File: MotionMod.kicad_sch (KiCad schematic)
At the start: 20 parts, among them J1 HC-SR04 Ultrasonic, J2 Photoelectric Module, J3 MCP4728 12 Bit DAC, J4 CV Out 1, J5 CV Out 2, J6 CV Out 3, J7 CV Out 4, J8 AMS1117 3.3v Regulator, J9 Eurorack Power, U1 TL074

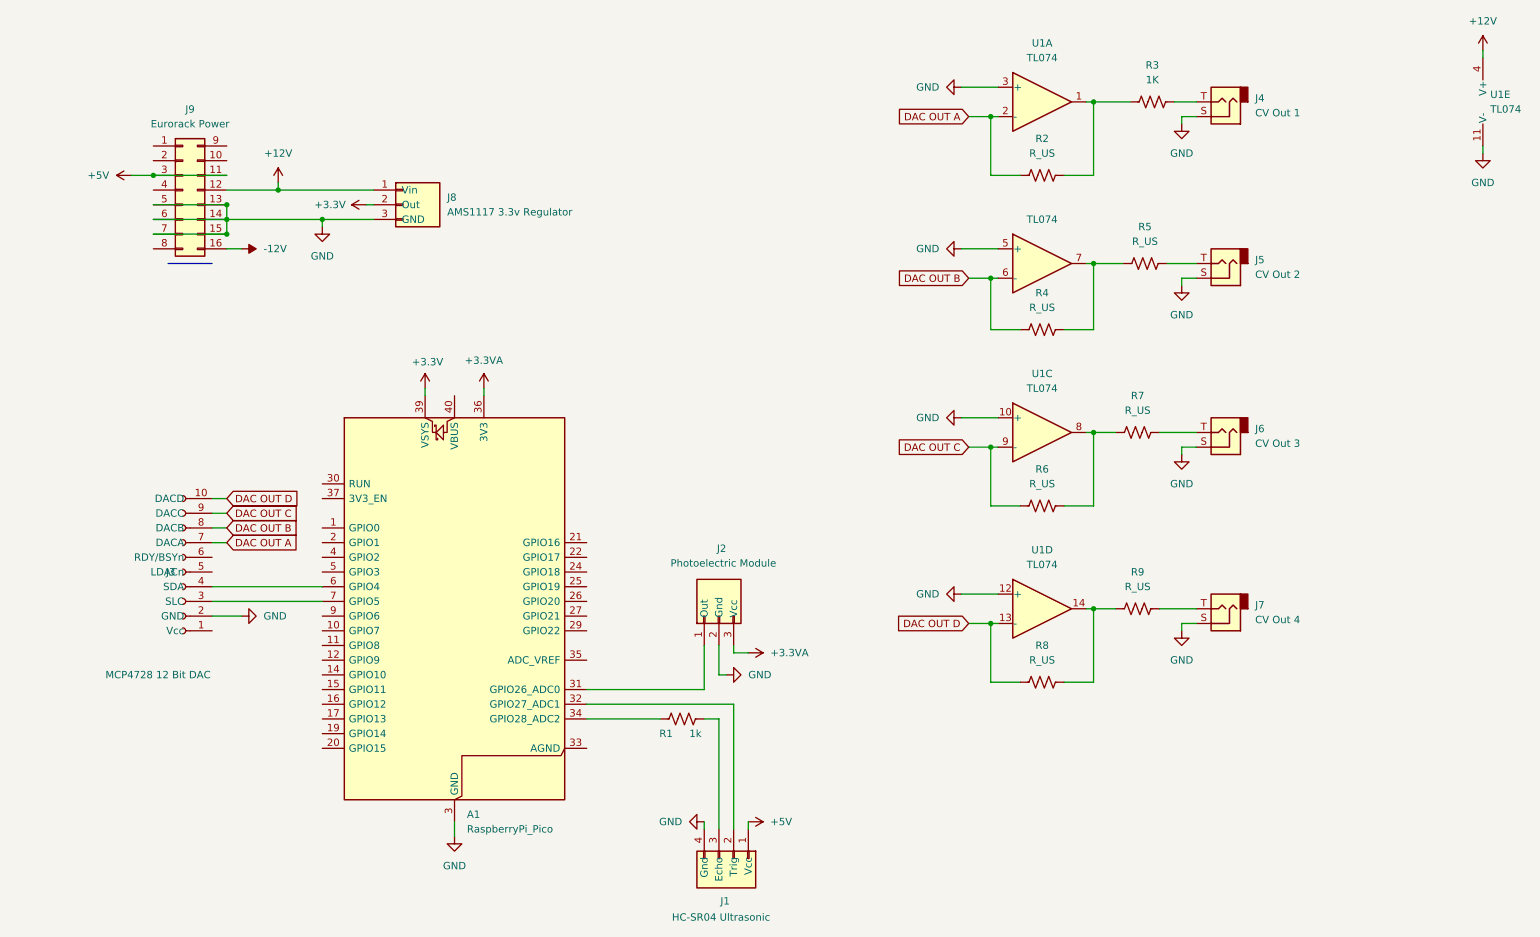
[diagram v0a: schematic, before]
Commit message: added sch image and pdf
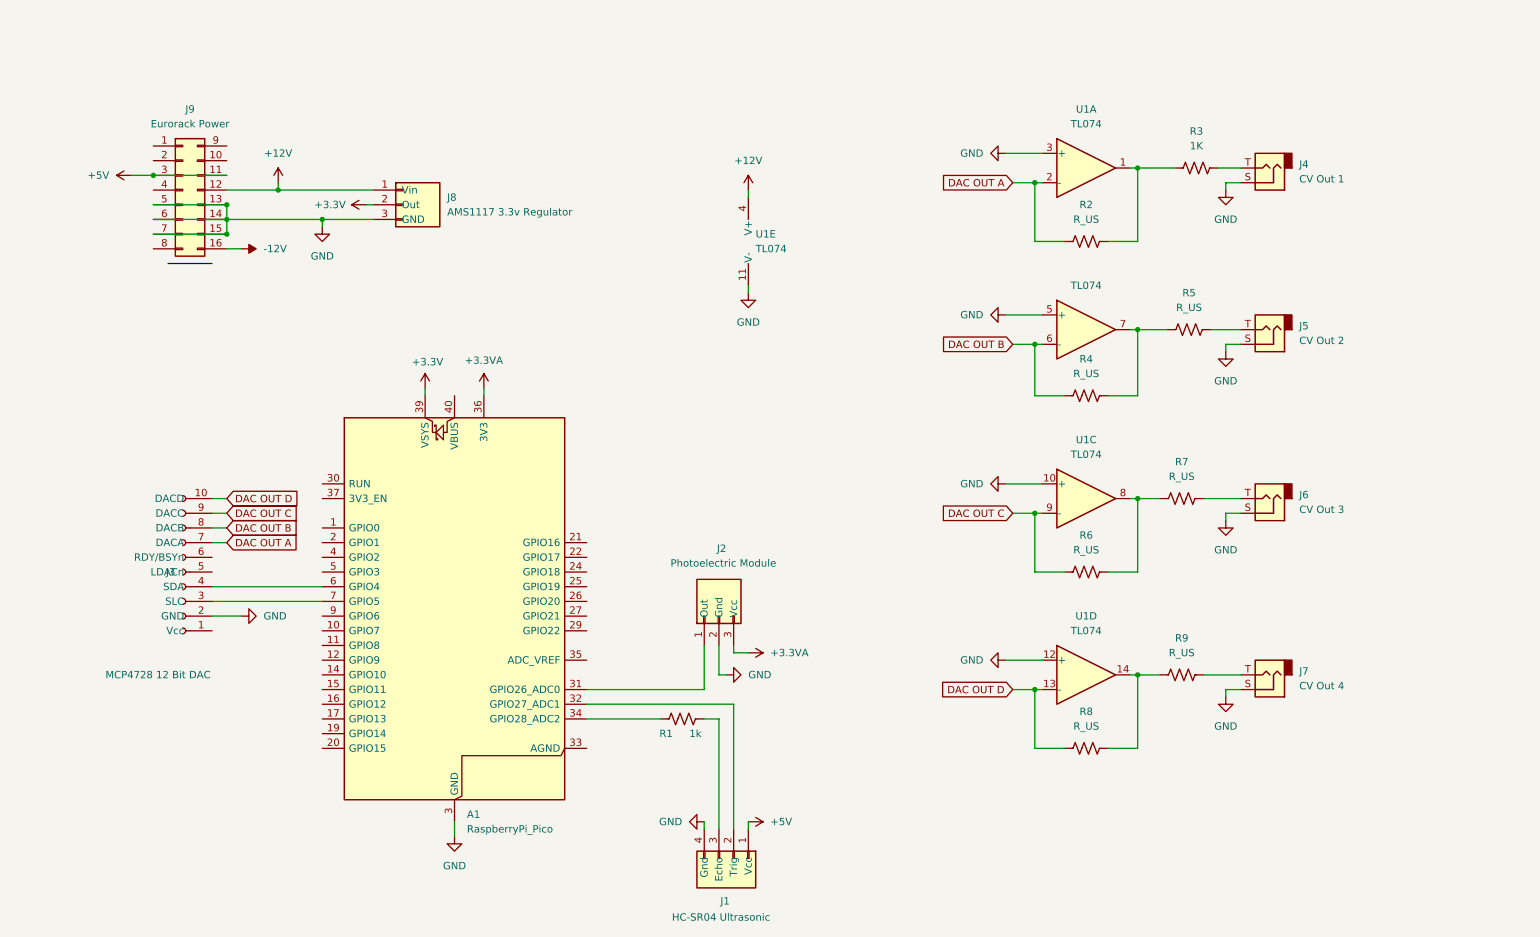
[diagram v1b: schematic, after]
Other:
- title: MotionMod - Movement based CV Generator -> ModSense - Movement based CV Generator for Eurorack
- moved on the sheet: J4, J5, J6, J7, R2, R3, R4, R5, R6, R7, R8, R9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

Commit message: final gerbers for v1
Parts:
- removed J1: HC-SR04 Ultrasonic, symbol Connector_Generic:Conn_01x04
- removed J2: Photoelectric Module, symbol Connector_Generic:Conn_01x03
- removed J4: CV Out 1, symbol Connector_Audio:AudioJack2
- removed J5: CV Out 2, symbol Connector_Audio:AudioJack2
- removed J6: CV Out 3, symbol Connector_Audio:AudioJack2
- removed J7: CV Out 4, symbol Connector_Audio:AudioJack2
- removed J8: AMS1117 3.3v Regulator, symbol Connector_Generic:Conn_01x03
- removed R1: 1k, symbol Device:R_US
- removed R3: 1K, symbol Device:R_US
- removed R5, R7, R9: R_US, symbol Device:R_US
- added J13: BottomSocket1, Connector_PinSocket_2.54mm:PinSocket_1x10_P2.54mm_Vertical, symbol Connector:Conn_01x10_Socket
- added J14: TopHeader1, Connector_PinHeader_2.54mm:PinHeader_1x10_P2.54mm_Vertical, symbol Connector:Conn_01x10_Pin
- added J4: BottomSocket2, Connector_PinSocket_2.54mm:PinSocket_1x10_P2.54mm_Vertical, symbol Connector:Conn_01x10_Socket
- added J5: TopHeader2, Connector_PinHeader_2.54mm:PinHeader_1x10_P2.54mm_Vertical, symbol Connector:Conn_01x10_Pin
- added R10, R12, R20, R21, R22: 10K, PCM_4ms_Resistor:R_Axial_DIN0207_L6.3mm_D2.5mm_P7.62mm_Horizontal, symbol Device:R_US
- added R11: 24K, PCM_4ms_Resistor:R_Axial_DIN0207_L6.3mm_D2.5mm_P7.62mm_Horizontal, symbol Device:R_US
- A1: footprint Module:RaspberryPi_Pico_Common_Unspecified -> Module:RaspberryPi_Pico_SMD_HandSolder
- J2: renamed from J9; value Eurorack Power -> Power; footprint (none) -> PCM_4ms_Connector:Pins_2x08_2.54mm_TH_EuroPower; symbol Connector_Generic:Conn_02x08_Top_Bottom -> PCM_4ms_Connector:Eurorack_Power_16pin_Unshrouded; Manufacturer (none) -> TAD; Part Number (none) -> 1-1602FBV0T; Specifications (none) -> Header, Male Pins, 2*8, spacing 2.54mm, straight pin
- J3: footprint (none) -> Connector_PinHeader_2.54mm:PinHeader_1x10_P2.54mm_Vertical
- R2, R4, R6, R8: value R_US -> 20K; footprint (none) -> PCM_4ms_Resistor:R_Axial_DIN0207_L6.3mm_D2.5mm_P7.62mm_Horizontal
- U1: footprint (none) -> Package_DIP:DIP-14_W7.62mm_LongPads
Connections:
- net +3.3V is gone; now on net +5V: A1.39 (VSYS)
- net +12V: now also J2.7 (12V), J2.8 (+12V); no longer J2.12 (Pin_12)
- net +5V: now also J2.5 (+12V), J2.6 (P6), J3.1 (Vcc), J4.10 (Pin_10), R11.1; no longer J2.11 (Pin_11), J2.3 (Pin_3)
- net -12V: now also J2.15 (-12V), U1.11 (V-)
- net DAC OUT A: now also R21.1; no longer R2.1, U1.2 (-)
- net DAC OUT B: now also R22.1; no longer R4.1, U1.6 (-)
- net DAC OUT C: now also R10.1; no longer R6.1, U1.9 (-)
- net DAC OUT D: now also R20.1; no longer R8.1, U1.13 (-)
- net GND: now also J2.10 (GND), J2.11 (GND), J2.12 (GND), J2.9 (GND), J4.9 (Pin_9), R12.1; no longer J2.15 (Pin_15), J2.5 (Pin_5), J2.6 (Pin_6), J2.7 (Pin_7), U1.10 (+), U1.11 (V-), U1.12 (+), U1.3 (+), U1.5 (+)
- net EncA_s: now reaches A1.1 (GPIO0)
- net EncA_s: now also J4.1 (Pin_1)
- net EncB_s: now reaches A1.2 (GPIO1)
- net EncB_s: now also J4.2 (Pin_2)
- net at A1.21 (GPIO16): now also J13.1 (Pin_1)
- net at A1.22 (GPIO17): now also J13.2 (Pin_2)
- net at A1.24 (GPIO18): now also J13.3 (Pin_3)
- net at A1.25 (GPIO19): now also J13.4 (Pin_4)
- net at A1.26 (GPIO20): now also J13.5 (Pin_5)
- net at A1.27 (GPIO21): now also J13.6 (Pin_6)
- net at A1.29 (GPIO22): now also J13.7 (Pin_7)
- net at A1.31 (GPIO26_ADC0): now also J13.8 (Pin_8)
- net at A1.32 (GPIO27_ADC1): now also J13.9 (Pin_9)
- net at A1.34 (GPIO28_ADC2): now also J13.10 (Pin_10)
- net EncSw_s: now reaches A1.4 (GPIO2)
- net EncSw_s: now also J4.3 (Pin_3)
- net at R2.2, U1.1: now also J4.4 (Pin_4)
- net at R6.2, U1.8: now also J4.6 (Pin_6)
- net at R4.2, U1.7: now also J4.5 (Pin_5)
- net at R8.2, U1.14: now also J4.7 (Pin_7)
- new net: R21.2, R6.1, U1.9 (-)
- new net: R22.2, R8.1, U1.13 (-)
- new net: R10.2, R2.1, U1.2 (-)
- new net: R20.2, R4.1, U1.6 (-)
- new net EncA_p: J5.1 (Pin_1)
- new net Top Board/5V: J5.10 (Pin_10)
- new net Top Board/CV1: J5.4 (Pin_4)
- new net Top Board/CV2: J5.5 (Pin_5)
- new net Top Board/CV3: J5.6 (Pin_6)
- new net Top Board/CV4: J5.7 (Pin_7)
- new net Top Board/DispA: J14.1 (Pin_1)
- new net Top Board/DispB: J14.2 (Pin_2)
- new net Top Board/DispC: J14.3 (Pin_3)
- new net Top Board/DispD: J14.4 (Pin_4)
- new net Top Board/DispDot: J14.8 (Pin_8)
- new net Top Board/DispE: J14.5 (Pin_5)
- new net Top Board/DispF: J14.6 (Pin_6)
- new net Top Board/DispG: J14.7 (Pin_7)
- new net Top Board/Echo: J14.10 (Pin_10)
- new net Top Board/EncB: J5.2 (Pin_2)
- new net Top Board/EncSW: J5.3 (Pin_3)
- new net Top Board/GND: J5.9 (Pin_9)
- new net Top Board/Trig: J14.9 (Pin_9)
- new net Vref: R11.2, R12.2, U1.10 (+), U1.12 (+), U1.3 (+), U1.5 (+)
- no-connect marks 0 -> 4
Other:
- added sheet Top Board (top.kicad_sch)
- moved on the sheet: A1, J3, R2, R4, R6, R8, U1A, U1C, U1D, U1E
